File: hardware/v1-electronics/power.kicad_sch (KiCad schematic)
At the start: 40 parts, among them IC1 TPS61288LRQQR, IC2 MP2721GRH-0000-Z, J1 Female USB-C USB2.0, J2 Female JST-VH, SW7 SW_SPDT

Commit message: doc(v1 hardware): finish schematics???
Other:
- note added: "Did the math, realized I don't have control system intuition/ background I have raw values I need to map to stardard resistor and capcitor size and values: - R_C = 14403.29218 Ω - C_C = 2.673 nF - C_P = 6.4152 pF These are the values after plugging in a real output cap (CL21A226MAQNNN): - R_C = 10020.57613 Ω - C_C = 2.673 nF - C_P = 2.88684 pF These are the standard values I'm going with: - R_C =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"
- note added: "Set V_out to 5v Datasheet Section 9.2.2.1 Because R2(R55) < 15kΩ we'll not be placing a noise reduction capacitor parallel to R2"
- note added: "This circuit is designed to provide the option to manually insure highest charging current possible, by reading the USB CC pins voltage I'm uncertain of the necessity of the 10kΩ resistors so I've made them optional."
- note added: "You should use the TPS61288L HotRod Lite variant Did a bunch of math to select a part for this. It resulted in me going with the recommended inductance Part selected: MWSA1004S-2R2MT"
- note removed: "Consider adding a fuel gauge ic: - i2c and led indictor - BQ27220"
- note removed: "Did a bunch of math to select a part for this. It resulted in me going with the recommended inductance"
- note removed: "Did the math, realized I don't have control system intuition. I have raw values I need to map to stardard resistor and capcitor size and values: - R_C = 14403.29218 Ω - C_C = 2.673 nF - C_P = 6.4152 pF These are the values after plugging in a real output cap (CL21A226MAQNNN): - R_C = 10020.57613 Ω - C_C = 2.673 nF - C_P = 2.88684 pF These are the standard values I'm going with: - R_C = 10 kΩ - C_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"
- note removed: "Have not done the math for this yet This involves control theory noise a big issue in these system"
- note removed: "Not sure if I should put a capacitor here. TI recommends putting a capacitor across the second resistor(R2) to protect against noise. The criteria is whiether R2 > or < 15kΩ. Though the datasheet has confliciting suggestions between Section 9.2.2.1 and Section 9.2"
- note removed: "Set V_out to 5v Datasheet Section 9.2.2.1"
- note removed: "This circuit is designed to provide the option to manually insure highest charging current possible, by reading the USB CC pins voltage How do zener diodes act when reversed biased? I don't think the 10kΩ resister are harmless or neceseary. Map scenarios for all USB pluggin cases."
- note removed: "You should use the TPS61288L HotRod Lite variant"
- note removed: "forgot what I was putting here Setup global reset How to handle power and analog grounds???"
- note removed: "is this the simplest power/usb-c module possible? Centralize the decoupling for +5V"
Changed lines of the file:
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@@
 	(rectangle
 		(start 439.42 149.86)
-		(end 487.68 205.74)
+		(end 487.68 180.34)
 		(stroke
 			(width 0.2)
@@
 	(rectangle
 		(start 353.06 149.86)
-		(end 393.7 205.74)
+		(end 393.7 210.82)
 		(stroke
 			(width 0.2)
@@
 	(rectangle
 		(start 396.24 149.86)
-		(end 436.88 243.84)
+		(end 436.88 231.14)
 		(stroke
 			(width 0.2)
@@
 	(rectangle
 		(start 25.4 152.4)
-		(end 142.24 236.22)
+		(end 142.24 228.6)
 		(stroke
 			(width 0.2)
@@
 		)
 	)
-	(text "This circuit is designed to provide the option\nto manually insure highest charging current\npossible, by reading the USB CC pins voltage\n\nHow do zener diodes act when reversed biased?\n\nI don't think the 10kΩ resister are harmless\nor neceseary.\n\nMap scenarios for all USB pluggin cases."
+	(text "This circuit is designed to provide the option\nto manually insure highest charging current\npossible, by reading the USB CC pins voltage\n\nI'm uncertain of the necessity of the 10kΩ\nresistors so I've made them optional."
 		(exclude_from_sim no)
 		(at 27.94 215.9 0)
@@
 		)
 	)
-	(text "Have not done the\nmath for this yet\n\nThis involves control theory\nnoise a big issue in these system"
-		(exclude_from_sim no)
-		(at 398.78 185.42 0)
-		(effects
-			(font
-				(size 1.27 1.27)
-			)
-			(justify left top)
-		)
-	)
-	(text "Not sure if I should\nput a capacitor here.\n\nTI recommends putting \na capacitor across the \nsecond resistor(R2) to \nprotect against noise.\n\nThe criteria is whiether \nR2 > or < 15kΩ. Though\nthe datasheet has \nconfliciting suggestions\nbetween Section 9.2.2.1\nand Section 9.2"
-		(exclude_from_sim no)
-		(at 459.74 167.64 0)
-		(effects
-			(font
-				(size 1.27 1.27)
-			)
-			(justify left top)
-		)
-	)
-	(text "Set V_out to 5v\nDatasheet Section 9.2.2.1"
-		(exclude_from_sim no)
-		(at 459.74 160.02 0)
-		(effects
-			(font
-				(size 1.27 1.27)
-			)
-			(justify left top)
-		)
-	)
-	(text "Did a bunch of math\nto select a part for\nthis. It resulted\nin me going with the\nrecommended inductance"
-		(exclude_from_sim no)
-		(at 358.14 193.04 0)
+	(text "Set V_out to 5v\nDatasheet Section 9.2.2.1\n\nBecause R2(R55) < 15kΩ \nwe'll not be placing a noise\nreduction capacitor parallel\nto  R2"
+		(exclude_from_sim no)
+		(at 459.74 154.94 0)
 		(effects
 			(font
@@
 		)
 	)
-	(text "You should use the \nTPS61288L HotRod Lite \nvariant"
+	(text "You should use the \nTPS61288L HotRod Lite \nvariant\n\nDid a bunch of math\nto select a part for\nthis. It resulted\nin me going with the\nrecommended inductance\n\nPart selected: MWSA1004S-2R2MT"
 		(exclude_from_sim no)
 		(at 358.14 185.42 0)
@@
 		)
 	)
-	(text "forgot what I was putting here\nSetup global reset\nHow to handle power and analog grounds???"
-		(exclude_from_sim no)
-		(at 15.24 279.4 0)
-		(effects
-			(font
-				(size 1.27 1.27)
-			)
-			(justify left top)
-		)
-	)
 	(text "*set to always on.\ntrying to control\nthis would be a power\nsquencing nightmare"
 		(exclude_from_sim no)
@@
 		)
 	)
-	(text "Did the math, realized I don't\nhave control system intuition.\n\nI have raw values I need to map to\nstardard resistor and capcitor size\nand values:\n- R_C = 14403.29218 Ω\n- C_C = 2.673 nF\n- C_P = 6.4152 pF\n\nThese are the values after \nplugging in a real output \ncap (CL21A226MAQNNN): \n- R_C = 10020.57613 Ω\n- C_C = 2.673 nF\n- C_P = 2.88684 pF\n\nThese are the standard \nvalues I'm going with:\n- R_C = 10 kΩ\n- C_C = 2.7 nF"
-		(exclude_from_sim no)
-		(at 398.78 198.12 0)
+	(text "Did the math, realized I don't\nhave control system intuition/\nbackground\n\nI have raw values I need to map to\nstardard resistor and capcitor size\nand values:\n- R_C = 14403.29218 Ω\n- C_C = 2.673 nF\n- C_P = 6.4152 pF\n\nThese are the values after \nplugging in a real output \ncap (CL21A226MAQNNN): \n- R_C = 10020.57613 Ω\n- C_C = 2.673 nF\n- C_P = 2.88684 pF\n\nThese are the standard \nvalues I'm going with:\n- R_C = 10 kΩ\n- C_C = 2.7 nF"
+		(exclude_from_sim no)
+		(at 398.78 185.42 0)
 		(effects
 			(font
@@
 			)
 			(justify left)
-		)
-	)
-	(text "is this the simplest power/usb-c module possible?\nCentralize the decoupling for +5V"
-		(exclude_from_sim no)
-		(at 15.24 274.32 0)
-		(effects
-			(font
-				(size 1.27 1.27)
-			)
-			(justify left top)
 		)
 	)
@@
 		)
 	)
-	(text "Consider adding a fuel gauge ic:\n- i2c and led indictor\n- BQ27220"
-		(exclude_from_sim no)
-		(at 71.12 279.4 0)
-		(effects
-			(font
-				(size 1.27 1.27)
-			)
-			(justify left top)
-		)
-	)
 	(text "Data Line ESD Protection"
 		(exclude_from_sim no)
@@
 	(text_box "Do I have enough protect on the USB contector?\nDo I still need to add resistors or pull up these lines?\nHave I properly set up the charger and regulator correctily?\nwhy can charge current be higher than input current in battery charger\nZener Diodes vs Schottky Diode for pin protection"
 		(exclude_from_sim no)
-		(at 12.7 259.08 0)
-		(size 91.44 27.94)
+		(at 12.7 271.78 0)
+		(size 91.44 14.3727)
 		(margins 0.9525 0.9525 0.9525 0.9525)
 		(stroke
@@
 	(text_box "Power Ratings per Critical Line\nUSB-C plug → Charger IC input:\n- max 5V @ 3A\n- must be configured\n\nUSB-C plug → Charger IC output:\n- Worst case output current draw 6A\n- Max output current 5A\n- Voltage range  3.125V ↔ 3.913V\n   default 3.7V \n\nBattery → Charger IC output:\n- Worst case discharge current draw 7.5A\n- Max discharge current 8A\n- Battery Voltage 3V ↔ 4.2V\n\nVoltage Regulator: Rating 5A, 5.5V\n- max 5V @ 4A\n\nFIRMWARE NOTE:\nPower scenarios must be accounted for in \nthe firware."
 		(exclude_from_sim no)
-		(at 121.92 12.7 0)
+		(at 119.38 12.7 0)
 		(size 71.12 73.66)
 		(margins 0.9525 0.9525 0.9525 0.9525)

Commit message: feat(v1 hardware): On/Off Load Switch implemented
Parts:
- removed SW7: SW_SPDT, symbol Switch:SW_SPDT
- added Q1: AON7423, symbol Alpha & Omega Semiconductor:AON7423
- added R44: 100kΩ, symbol Device:R_Small
- added R48: 1kΩ, symbol Device:R_Small
- added SW7: 2TED1M2RES, symbol Switch:SW_Push_DPDT
- gave numbers to parts that had none: 2
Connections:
- net DGND: now also SW7.1 (A), SW7.4 (A)
- net V_IN_TPS: now also Q1.5 (D), Q1.6 (D), Q1.7 (D), Q1.8 (D), Q1.9 (D)
- net V_OUT_MP: now also Q1.1 (S), Q1.2 (S), Q1.3 (S), R44.1
- new net: R48.2, SW7.2 (B), SW7.5 (B)
- new net: Q1.4 (G), R44.2, R48.1
- no-connect marks 1 -> 3
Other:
- note added: "Consider using USBLC6-4SC6 instead of using your own over voltage protection USBLC6-4SC6 jlcpcb"
- note added: "Protected Cell for the battery (18650) Polyfuse Rethink how the the tempature sensors work with the new battery plug"
- moved on the sheet: C45, C46, C47, C48, C49, C50, D65, D87, D88, D89, J2, JP5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

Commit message: feat(v1 hardware): place foot prints
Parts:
- added C54: 10μF, Capacitor_SMD:C_0805_2012Metric, symbol Device:C_Small
- C37, C38, C39, C41, C44, C46, C49: footprint (none) -> Capacitor_SMD:C_0805_2012Metric
- C40, C50: value 20μF -> 10μF; footprint (none) -> Capacitor_SMD:C_0805_2012Metric
- C42, C48: value 0.10μF -> 0.1μF; footprint (none) -> Capacitor_SMD:C_0402_1005Metric
- C43: footprint (none) -> Capacitor_SMD:C_0402_1005Metric
- C45: value 2.7nF -> 2.2nF; footprint (none) -> Capacitor_SMD:C_0805_2012Metric
- C47: footprint (none) -> Capacitor_SMD:C_1206_3216Metric
- D64: footprint SOT95P280X145-6N -> STMicroelectronics:SOT95P280X145-6N
- D88, D89: footprint (none) -> Diode_SMD:D_SOD-123
- FL1: footprint EXC14CE900U -> (none)
- IC1: footprint PTPS61288RQQR -> Texas Instruments:PTPS61288RQQR
- J1: footprint (none) -> Connector_USB:USB_C_Receptacle_GCT_USB4085
- J2: value Female JST-VH -> XT30PW-M; footprint (none) -> Connector_AMASS:AMASS_XT30PW-M_1x02_P2.50mm_Horizontal
- JP5, JP6: footprint (none) -> Connector_PinHeader_2.54mm:PinHeader_1x02_P2.54mm_Vertical
- L1: value 560nH -> 1μH
- L2: footprint (none) -> Inductor_SMD:L_Sunlord_MWSA1005S
- R44, R48: footprint (none) -> Resistor_SMD:R_1206_3216Metric; now in the parts list
- R49, R51, R52, R53, R57, R60, R61: footprint (none) -> Resistor_SMD:R_0805_2012Metric
- R50: value 44kΩ -> 22kΩ; footprint (none) -> Resistor_SMD:R_0805_2012Metric
- R55: value 6kΩ -> 3kΩ; footprint (none) -> Resistor_SMD:R_0805_2012Metric
- R56: value 10kΩ -> 15kΩ; footprint (none) -> Resistor_SMD:R_0805_2012Metric
- SW7: now in the parts list
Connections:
- net DGND: now also C54.2
- net V_OUT_MP: now also C54.1
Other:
- note added: "Protected Cell for the battery (18650) Polyfuse Rethink how the the tempature sensors work with the new battery plug For now we'll use XT30PW-M, but if We decide to use a 3Pin solution we'll use the MR30PW-M. At the time of writing this we'll be using a unprotected raw power lipo."
- note added: "Redid my calculations and selected 1μH @ 10A I_sat Check the footprint of this device again"
- note removed: "Consider using USBLC6-4SC6 instead of using your own over voltage protection USBLC6-4SC6 jlcpcb"
- note removed: "Protected Cell for the battery (18650) Polyfuse Rethink how the the tempature sensors work with the new battery plug"
- note removed: "calculations the value of the inductor for our usage is about 509 nH, for part finding perposes 560 nH part."
- moved on the sheet: C45, D88, D89, JP6, R49, R51, R56, R61

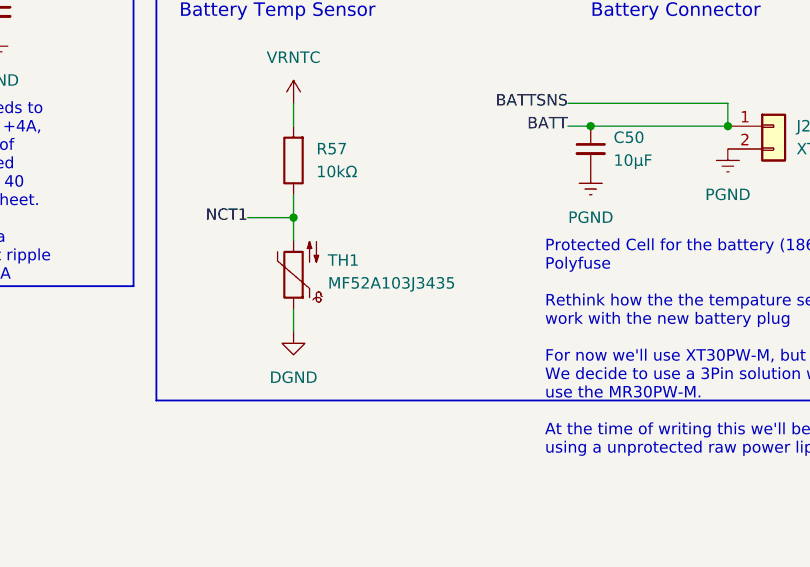
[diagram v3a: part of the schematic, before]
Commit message: feat(v1 hardware): all power train components foot prints selected
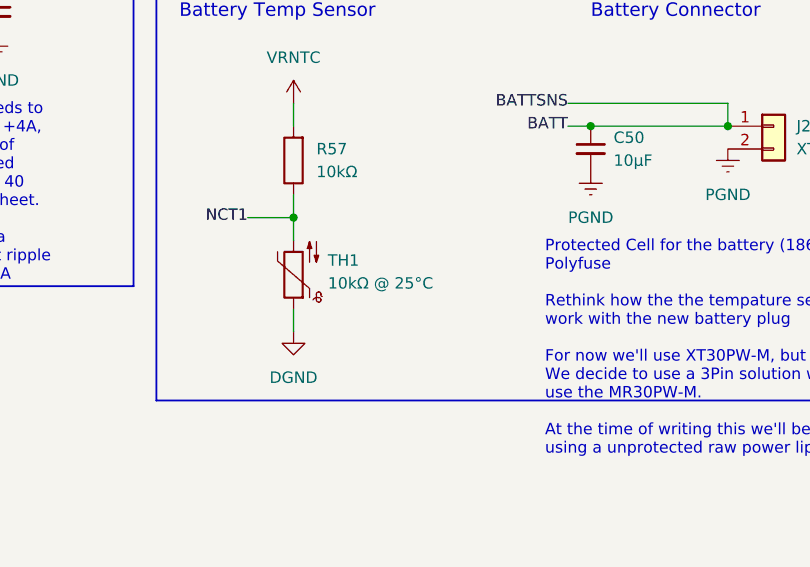
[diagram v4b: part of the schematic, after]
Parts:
- D65, D87: footprint (none) -> LED_SMD:LED_0805_2012Metric
- FL1: footprint (none) -> Panasonic:EXC14CE900U
- IC2: footprint (none) -> Monolithic Power Systems:QFN-22_MP2721_MNP
- L1: footprint (none) -> Inductor_SMD:L_Changjiang_FTC404030S
- Q1: footprint (none) -> Alpha & Omega Semiconductor:AON7423
- SW7: footprint (none) -> Dailywell:2TED3M6RES
- TH1: value MF52A103J3435 -> 10kΩ @ 25°C; footprint (none) -> Vishay Intertech:NTCLE413E2103F102L
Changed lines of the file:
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@@
 			)
 		)
-		(property "Footprint" ""
+		(property "Footprint" "Inductor_SMD:L_Changjiang_FTC404030S"
 			(at 241.3 185.42 0)
 			(hide yes)
@@
 			)
 		)
-		(property "Footprint" ""
+		(property "Footprint" "Dailywell:2TED3M6RES"
 			(at 340.36 137.16 0)
 			(hide yes)
@@
 			)
 		)
-		(property "Footprint" ""
+		(property "Footprint" "Alpha & Omega Semiconductor:AON7423"
 			(at 337.82 96.52 0)
 			(hide yes)
@@
 			)
 		)
-		(property "Description" ""
+		(property "Description" "part selected: AON7423"
 			(at 337.82 96.52 0)
 			(hide yes)
@@
 			)
 		)
-		(property "Footprint" ""
+		(property "Footprint" "LED_SMD:LED_0805_2012Metric"
 			(at 322.58 185.42 90)
 			(hide yes)
@@
 			)
 		)
-		(property "Description" "Light emitting diode, small symbol, filled shape"
+		(property "Description" "part selected: KT-0805G"
 			(at 322.58 185.42 0)
 			(hide yes)
@@
 			)
 		)
-		(property "Footprint" ""
+		(property "Footprint" "Panasonic:EXC14CE900U"
 			(at 127.508 188.646 0)
 			(hide yes)
@@
 			)
 		)
-		(property "Footprint" ""
+		(property "Footprint" "LED_SMD:LED_0805_2012Metric"
 			(at 322.58 187.96 90)
 			(hide yes)
@@
 			)
 		)
-		(property "Description" "Light emitting diode, small symbol, filled shape"
+		(property "Description" "part selected: KT-0805W"
 			(at 322.58 187.96 0)
 			(hide yes)
@@
 			)
 		)
-		(property "Footprint" ""
+		(property "Footprint" "Monolithic Power Systems:QFN-22_MP2721_MNP"
 			(at 276.86 88.9 0)
 			(hide yes)
@@
 			)
 		)
-		(property "Value" "MF52A103J3435"
+		(property "Value" "10kΩ @ 25°C"
 			(at 275.59 246.0624 0)
 			(show_name no)
@@
 			)
 		)
-		(property "Footprint" ""
+		(property "Footprint" "Vishay Intertech:NTCLE413E2103F102L"
 			(at 271.78 246.38 0)
 			(hide yes)
@@
 			)
 		)
-		(property "Description" "Temperature dependent resistor, negative temperature coefficient"
+		(property "Description" "part selected: NTCLE413E2103F102L"
 			(at 271.78 245.11 0)
 			(hide yes)

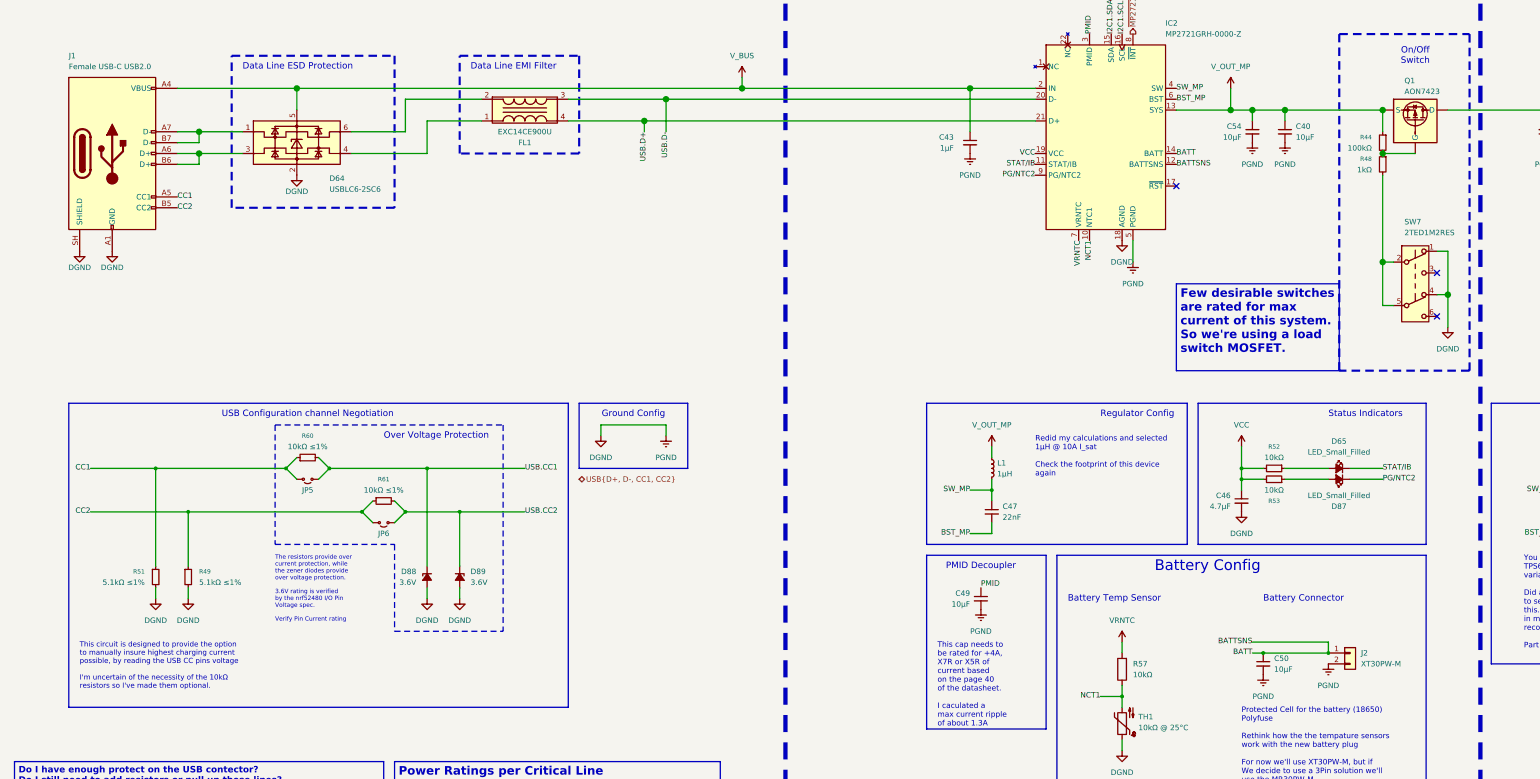
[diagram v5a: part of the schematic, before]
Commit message: feat(v1 hardware): aligned schematic symbols with pcb footprints
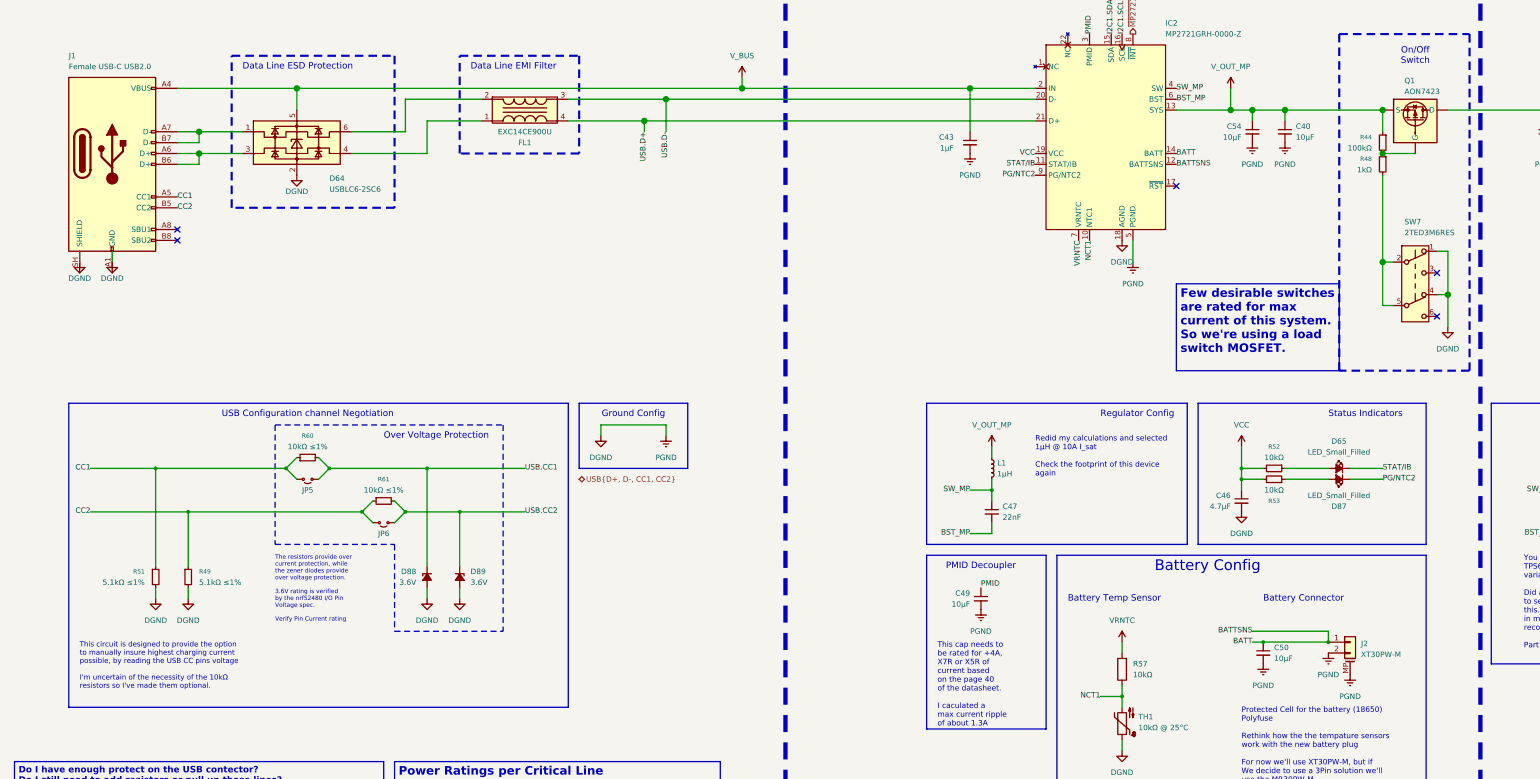
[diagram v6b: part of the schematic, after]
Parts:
- J2: symbol Connector_Generic:Conn_01x02 -> Connector_Generic_MountingPin:Conn_01x02_MountingPin
- SW7: value 2TED1M2RES -> 2TED3M6RES
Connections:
- net DGND: now also J2.MP (MountPin); no longer J1.A1 (GND), J1.A12 (GND), J1.B1 (GND), J1.B12 (GND), J1.SH (SHIELD)
- new net: J1.A1 (GND), J1.A12 (GND), J1.B1 (GND), J1.B12 (GND)
- no-connect marks 3 -> 5
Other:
- moved on the sheet: C50

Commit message: feat(v1 hardware): transfer to ergogen layout
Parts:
- renumbered D64 to D0, D65 to D90
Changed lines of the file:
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@@
 		(title "Slack")
 		(date "2026-07-25")
-		(rev "A.0.5")
+		(rev "A.0.7")
 	)
 	(rectangle
@@
 		(in_pos_files yes)
 		(dnp no)
-		(property "Reference" "D64"
+		(property "Reference" "D0"
 			(at 86.36 116.84 0)
 			(show_name no)
@@
 			(project "slack"
 				(path "/504df67f-9f45-483f-90c8-f14c049b6b02/a24a3d75-e466-4feb-b98a-50e4b7a182a1"
-					(reference "D64")
+					(reference "D0")
 					(unit 1)
 				)
@@
 		(in_pos_files yes)
 		(dnp no)
-		(property "Reference" "D65"
+		(property "Reference" "D90"
 			(at 322.5165 179.07 0)
 			(show_name no)
@@
 			(project "slack"
 				(path "/504df67f-9f45-483f-90c8-f14c049b6b02/a24a3d75-e466-4feb-b98a-50e4b7a182a1"
-					(reference "D65")
+					(reference "D90")
 					(unit 1)
 				)
